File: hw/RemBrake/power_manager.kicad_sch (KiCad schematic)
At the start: 29 parts, among them Q10 BC337, Q11 BC847, Q12 BC847, Q13 SiS415DNT, Q14 BC337, U7 LTC2943IDD#TRPBF, U8 MAX40200AUK

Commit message: removed hopefully last redundant components and updated versions of pcb and schematics
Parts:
- R50: now left out of the parts list

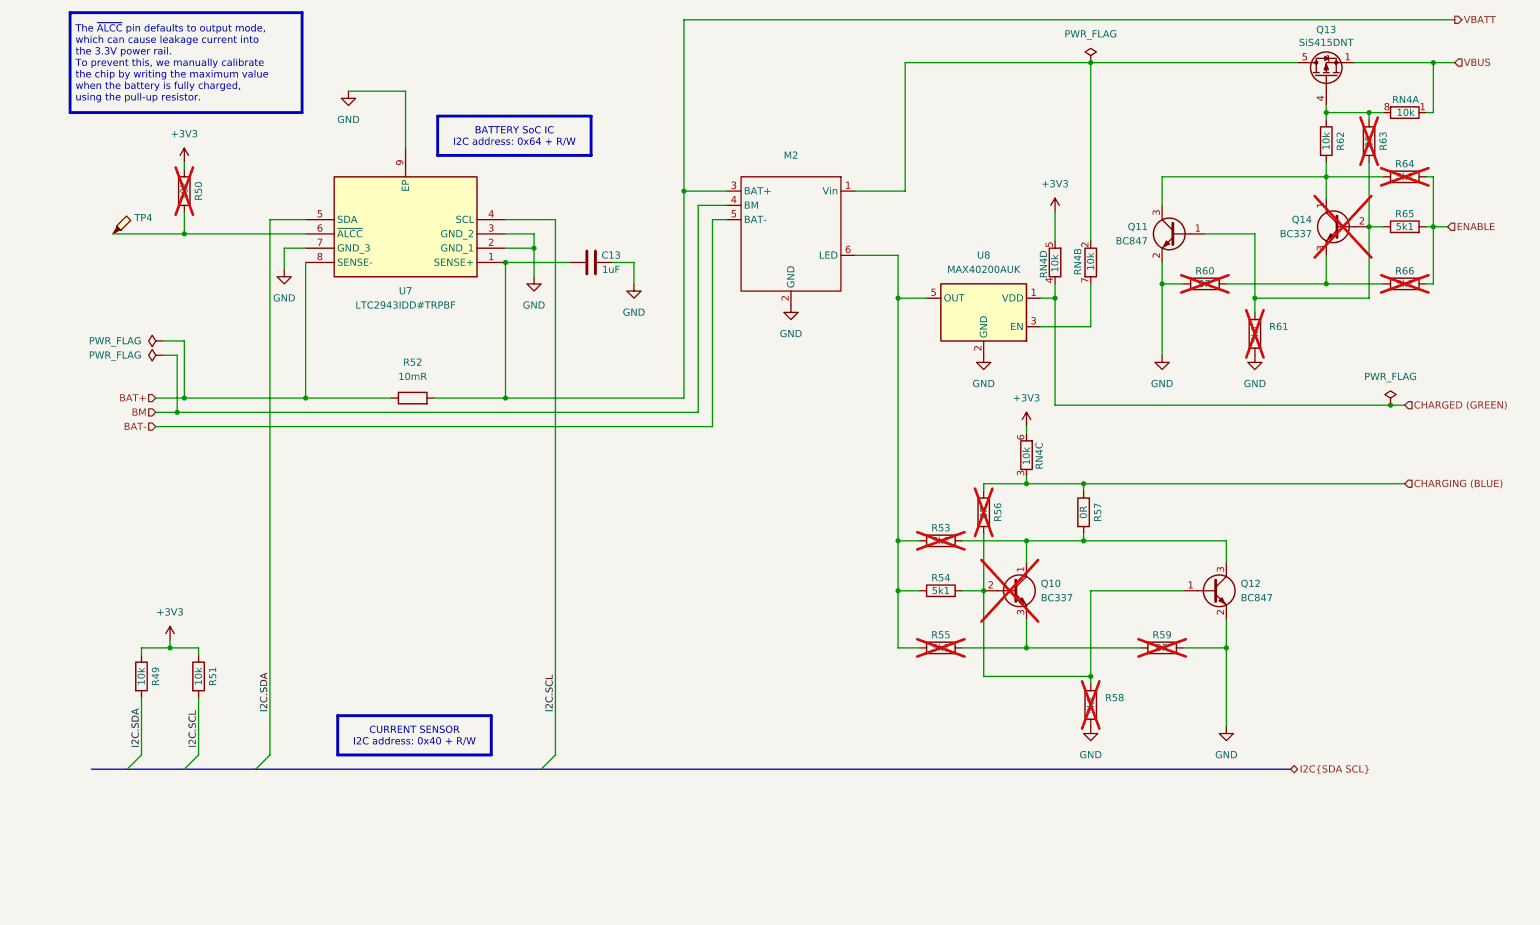
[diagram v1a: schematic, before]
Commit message: updated pcb and added Notes about possible faults
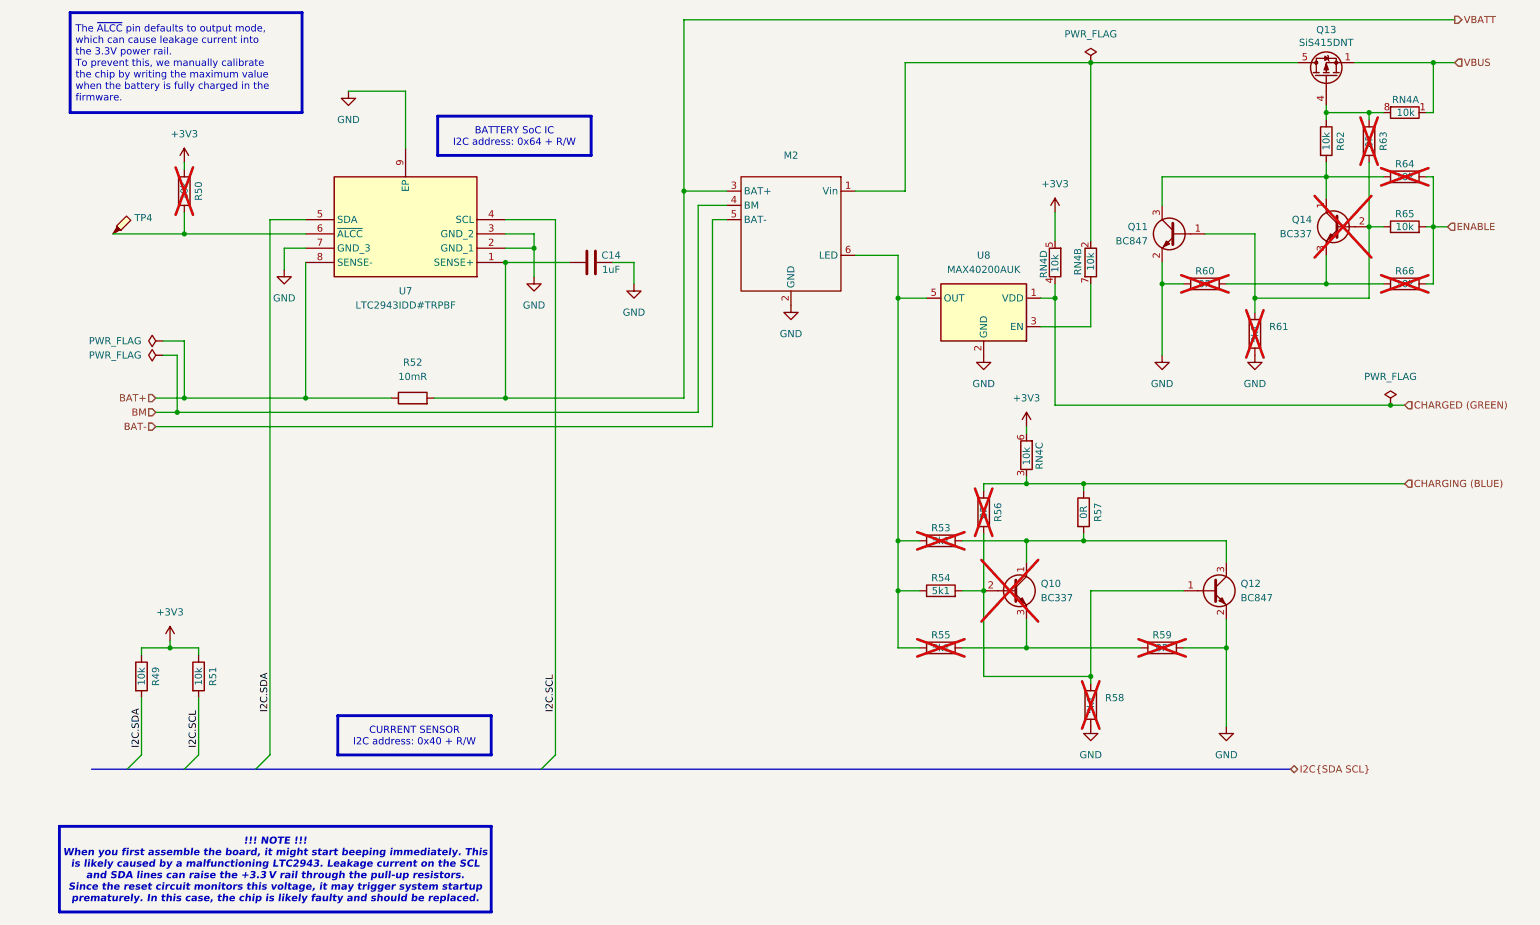
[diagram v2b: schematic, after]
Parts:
- R64, R65, R66: value 5k1 -> 10k
- renumbered C13 to C14
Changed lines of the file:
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@@
 		(company "Pacner Bros Tech")
 	)
+	(text_box "!!! NOTE !!!\nWhen you first assemble the board, it might start beeping immediately. This is likely caused by a malfunctioning LTC2943. Leakage current on the SCL and SDA lines can raise the +3.3 V rail through the pull-up resistors. Since the reset circuit monitors this voltage, it may trigger system startup prematurely. In this case, the chip is likely faulty and should be replaced."
+		(exclude_from_sim no)
+		(at 22.225 163.83 0)
+		(size 76.835 15.24)
+		(margins 0.9525 0.9525 0.9525 0.9525)
+		(stroke
+			(width 0.508)
+			(type solid)
+			(color 128 63 0 1)
+		)
+		(fill
+			(type color)
+			(color 255 255 153 1)
+		)
+		(effects
+			(font
+				(size 1.27 1.27)
+				(thickness 0.254)
+				(bold yes)
+				(italic yes)
+			)
+		)
+	)
 	(text_box "BATTERY SoC IC\nI2C address: 0x64 + R/W"
 		(exclude_from_sim no)
@@
 		)
 	)
-	(text_box "The ~{ALCC} pin defaults to output mode, \nwhich can cause leakage current into \nthe 3.3V power rail.\nTo prevent this, we manually calibrate \nthe chip by writing the maximum value \nwhen the battery is fully charged, \nusing the pull-up resistor."
+	(text_box "The ~{ALCC} pin defaults to output mode, \nwhich can cause leakage current into \nthe 3.3V power rail.\nTo prevent this, we manually calibrate \nthe chip by writing the maximum value \nwhen the battery is fully charged in the firmware."
 		(exclude_from_sim no)
 		(at 24.13 19.05 0)
@@
 		(on_board yes)
 		(dnp no)
-		(property "Reference" "C13"
+		(property "Reference" "C14"
 			(at 120.396 62.23 90)
 			(effects
@@
 			(project "RemBrake"
 				(path "/e6d4ae5b-c9d7-4cbe-b288-c929fdf55a75/65dd8b54-1c0a-4683-aa46-51c439d49612"
-					(reference "C13")
+					(reference "C14")
 					(unit 1)
 				)
@@
 			)
 		)
-		(property "Value" "5k1"
+		(property "Value" "10k"
 			(at 261.62 67.31 90)
 			(effects
@@
 			)
 		)
-		(property "Value" "5k1"
+		(property "Value" "10k"
 			(at 261.62 57.15 90)
 			(effects
@@
 			)
 		)
-		(property "Value" "5k1"
+		(property "Value" "10k"
 			(at 261.62 48.26 90)
 			(effects

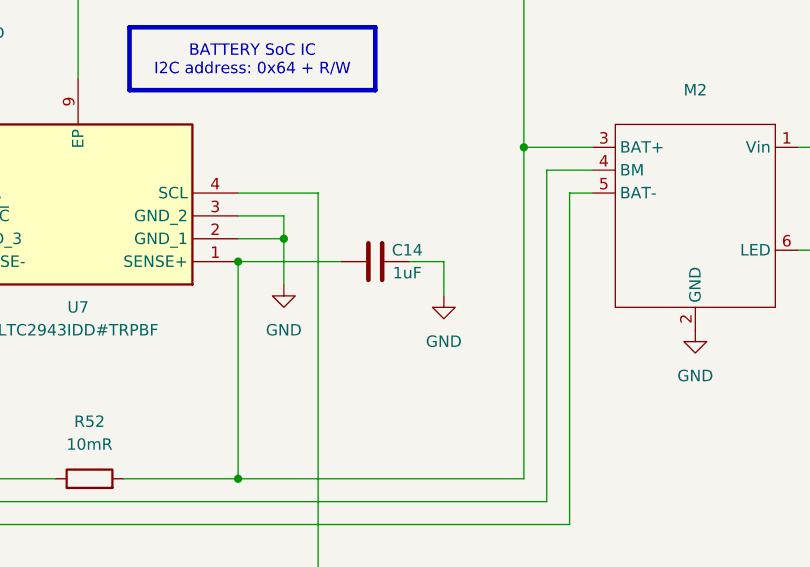
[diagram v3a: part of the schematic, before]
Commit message: updated BOM list and reduced number of different capacitors and resistors
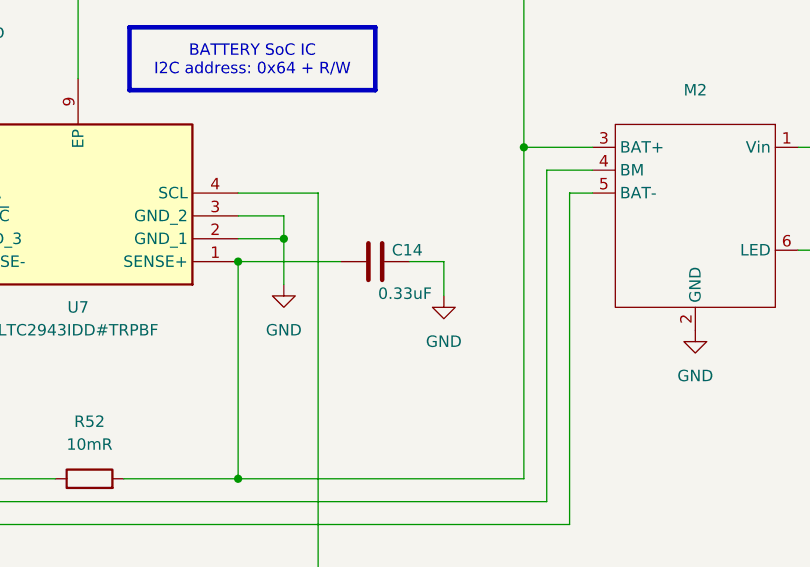
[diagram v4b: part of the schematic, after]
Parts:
- C14: value 1uF -> 0.33uF
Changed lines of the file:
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@@
 			)
 		)
-		(property "Value" "1uF"
-			(at 120.396 64.77 90)
+		(property "Value" "0.33uF"
+			(at 120.142 67.056 90)
 			(effects
 				(font
